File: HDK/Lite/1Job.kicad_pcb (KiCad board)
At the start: 2 copper layers, 48 x 48 mm, 43 parts, among them J101 USB C, J201 TERM, J301 A1-SEL, J302 SSR, J303 CAN, J304 ANA, J305 PWR, J306 DIO, U101 STM32G030F6Px, U102 STM32G030K6Tx, U103 AMS1117-3.3, U104 CH340N, U105 USBLC6-4SC6, U201 SN65HVD230, U202 MCP2518FD, U301 KAQY214, Y201 40MHz

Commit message: updated 1 Job, WIP
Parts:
- removed C106: 100n, Capacitor_SMD:C_0603_1608Metric
- removed D101: 1N4148W, Diode_SMD:D_SOD-123
- removed J101: USB C, Connector_USB:USB_C_Receptacle_HRO_TYPE-C-31-M-12
- removed J302: SSR, Connector_JST:JST_XH_B2B-XH-AM_1x02_P2.50mm_Vertical
- removed J303: CAN, Connector_JST:JST_XH_B2B-XH-AM_1x02_P2.50mm_Vertical
- removed J304: ANA, Connector_JST:JST_PH_S3B-PH-K_1x03_P2.00mm_Horizontal
- removed J305: PWR, Connector_JST:JST_XH_B2B-XH-AM_1x02_P2.50mm_Vertical
- removed J306: DIO, Connector_JST:JST_PH_S3B-PH-K_1x03_P2.00mm_Horizontal
- removed R101, R102, R103, R104, R302, R303, R304, R306: 5.1k, Resistor_SMD:R_0603_1608Metric
- removed R301, R305: 10k, Resistor_SMD:R_0603_1608Metric
- removed R307: 330, Resistor_SMD:R_0603_1608Metric
- removed the REF** at (117.0, 106.8)
- removed U103: AMS1117-3.3, Package_TO_SOT_SMD:SOT-223-3_TabPin2
- removed U104: CH340N, Package_SO:SOIC-8_3.9x4.9mm_P1.27mm
- removed U105: USBLC6-4SC6, Package_TO_SOT_SMD:SOT-23-6
- removed U301: KAQY214, Package_SO:SOP-4_3.8x4.1mm_P2.54mm
- added C401: 100n, Capacitor_SMD:C_0603_1608Metric, F.Cu at (108.1, 103.0)
- added D401: B5819W, Diode_SMD:D_SOD-123, F.Cu at (102.0, 115.8)
- added D402: B5819W, Diode_SMD:D_SOD-123, F.Cu at (110.7, 111.8)
- added J401: SSR, Connector_JST:JST_PH_S2B-PH-K_1x02_P2.00mm_Horizontal, F.Cu at (110.8, 80.5)
- added J402: CAN, Connector_JST:JST_PH_S2B-PH-K_1x02_P2.00mm_Horizontal, F.Cu at (87.2, 119.5)
- added J403: ANA, Connector_JST:JST_PH_S3B-PH-K_1x03_P2.00mm_Horizontal, F.Cu at (102.3, 80.5)
- added J404: PWR, Connector_JST:JST_PH_S2B-PH-K_1x02_P2.00mm_Horizontal, F.Cu at (100.4, 119.5)
- added J405: DIO, Connector_JST:JST_PH_S3B-PH-K_1x03_P2.00mm_Horizontal, F.Cu at (92.0, 80.5)
- added J406: A1-SEL, Connector_PinHeader_2.54mm:PinHeader_1x03_P2.54mm_Vertical, F.Cu at (102.8, 84.9)
- added J407: USB C, Connector_USB:USB_C_Receptacle_HRO_TYPE-C-31-M-12, F.Cu at (121.5, 107.5)
- added R401: 10k, Resistor_SMD:R_0603_1608Metric, F.Cu at (102.4, 88.4)
- added R402: 5.1k, Resistor_SMD:R_0603_1608Metric, F.Cu at (102.4, 90.0)
- added R403: 5.1k, Resistor_SMD:R_0603_1608Metric, F.Cu at (102.4, 91.6)
- added R404: 5.1k, Resistor_SMD:R_0603_1608Metric, F.Cu at (99.0, 88.4)
- added R405: 10k, Resistor_SMD:R_0603_1608Metric, F.Cu at (99.0, 91.6)
- added R406: 5.1k, Resistor_SMD:R_0603_1608Metric, F.Cu at (99.0, 90.0)
- added R407: 330, Resistor_SMD:R_0603_1608Metric, F.Cu at (107.4, 91.3)
- added R408: 5.1k, Resistor_SMD:R_0603_1608Metric, F.Cu at (117.8, 113.8)
- added R409: 5.1k, Resistor_SMD:R_0603_1608Metric, F.Cu at (117.8, 115.4)
- added REF**: SW_SPST_PTS810, Button_Switch_SMD:SW_SPST_PTS810, F.Cu at (103.0, 99.9)
- added U401: KAQY214, Package_SO:SOP-4_3.8x4.1mm_P2.54mm, F.Cu at (107.8, 86.7)
- added U402: CH340N, Package_SO:SOIC-8_3.9x4.9mm_P1.27mm, F.Cu at (110.6, 107.3)
- J301: value A1-SEL -> GT-TF003-H0185-02; footprint Connector_PinHeader_2.54mm:PinHeader_1x03_P2.54mm_Vertical -> Connector_Card:microSD_HC_Molex_104031-0811
- U101: value STM32G030F6Px -> STM32G030K6Tx; footprint Package_SO:TSSOP-20_4.4x6.5mm_P0.65mm -> Package_QFP:LQFP-32_7x7mm_P0.8mm
- U102: value STM32G030K6Tx -> AMS1117-3.3; footprint Package_QFP:LQFP-32_7x7mm_P0.8mm -> Package_TO_SOT_SMD:SOT-223-3_TabPin2
- moved J201 55.2 mm to (95.3, 122.0), turned to 180 degrees
- moved U201 53.7 mm to (88.4, 113.4), turned to -90 degrees
- moved Y201 53.3 mm to (97.0, 104.4)
- moved U202 53.2 mm to (89.0, 104.3), turned to 90 degrees
- moved C201 50.9 mm to (85.2, 99.0), turned to 90 degrees
- moved C202 47.2 mm to (88.5, 108.8)
- moved C104 45.6 mm to (114.7, 122.1), turned to 0 degrees
- moved C105 44.9 mm to (114.5, 120.2), turned to 0 degrees
- moved R201 43.7 mm to (92.0, 115.0), turned to -90 degrees
- moved J301 43.5 mm to (116.9, 90.9), turned to -90 degrees
- moved R202 43.1 mm to (92.6, 120.4), turned to -90 degrees
- moved C204 40.8 mm to (96.7, 101.8)
- moved C203 39.3 mm to (96.7, 107.0)
- moved U102 38.8 mm to (109.3, 118.9), turned to -90 degrees
- moved C102 29.5 mm to (106.2, 113.4), turned to 180 degrees
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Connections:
- net /CanBus/CAN_+ renamed /CAN_+
- net /CanBus/CAN_- renamed /CAN_-
- net /PA0 renamed /ANA_0
- net /PB0 renamed /CAN_CS2
- net /PB3 renamed /PC6
- net /UART2_RX renamed /PA3
- net /UART2_TX renamed /PA2
- C203 pad 1: /CanBus/OSC_OUT -> /CanBus/OSC_IN
- C204 pad 1: /CanBus/OSC_IN -> /CanBus/OSC_OUT
- J301 pad 1: /1JIO/A1_DIV-03V -> unconnected-(J301-DAT2-Pad1)
- J301 pad 2: /1JIO/A1_DIV-12V -> /PA8
- J301 pad 3: /1JIO/A1_DIV-05V -> /PA6
- U101 pad 1: /PB7 -> /I2C1_SDA
- U101 pad 12: /SPI1_SCK -> /PA5
- U101 pad 13: /SPI1_MISO -> /PA6
- U101 pad 14: /SPI1_MOSI -> /PA7
- U101 pad 16: /I2C_SCL -> /DO_SSR
- U101 pad 17: /I2C_SDA -> /PB2
- U101 pad 18: /SWDIO -> /PA8
- U101 pad 19: /SWCLK -> /I2C1_SCL
- U101 pad 8: /PA1 -> /ANA_1
- U102 pad 1: unconnected-(U102-PB9-Pad1) -> GND
- U102 pad 2: unconnected-(U102-PC14-Pad2) -> +3V3
- U102 pad 3: unconnected-(U102-PC15-Pad3) -> VCC
- U202 pad 10: /CanBus/SPI_SCK -> /PB8
- U202 pad 11: /CanBus/SPI_MOSI -> /PB2
- U202 pad 12: /CanBus/SPI_MISO -> /PA10
- U202 pad 13: /CanBus/SPI_CANCS -> /CAN_CS1
- U202 pad 4: unconnected-(U202-~{INT}-Pad4) -> /PB5
- U202 pad 8: unconnected-(U202-~{INT1}/GPIO1-Pad8) -> /CanBus/~{INT1}
- U202 pad 9: unconnected-(U202-~{INT0}/GPIO0/XSTBY-Pad9) -> /CanBus/~{INT0}
- Y201 pad 1: /CanBus/OSC_OUT -> /CanBus/OSC_IN
- Y201 pad 4: /CanBus/OSC_IN -> /CanBus/OSC_OUT
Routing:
- net +3V3: track 0.00 -> 138.1 mm, vias 0 -> 6
- net /PA5: track 0.00 -> 42.6 mm, vias 0 -> 2
- net /PA7: track 0.00 -> 39.9 mm, vias 0 -> 2
- net /PA14: track 0.00 -> 37.0 mm, vias 0 -> 2
- net /PA8: track 0.00 -> 36.9 mm, vias 0 -> 2
- net /PA13: track 0.00 -> 36.5 mm, vias 0 -> 2
- net /PA6: track 0.00 -> 35.8 mm, vias 0 -> 2
- net /SWDIO: track 31.8 -> 0.00 mm, vias 2 -> 0
- net /SWCLK: track 30.6 -> 0.00 mm, vias 2 -> 0
- net /DO_SSR: track 0.00 -> 30.3 mm, vias 0 -> 2
- net GND: track 5.84 -> 33.1 mm, vias 5 -> 19
- net /PB6: track 0.00 -> 22.3 mm, vias 0 -> 2
- net /PB7: track 0.00 -> 22.2 mm, vias 0 -> 2
- net /ANA_1: track 0.00 -> 17.9 mm, vias 0 -> 2
- net /~{NRST}: track 0.00 -> 17.1 mm, vias 0 -> 2
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- added copper zone on F.Cu, net +3V3
- added copper zone on F.Cu, net VCC

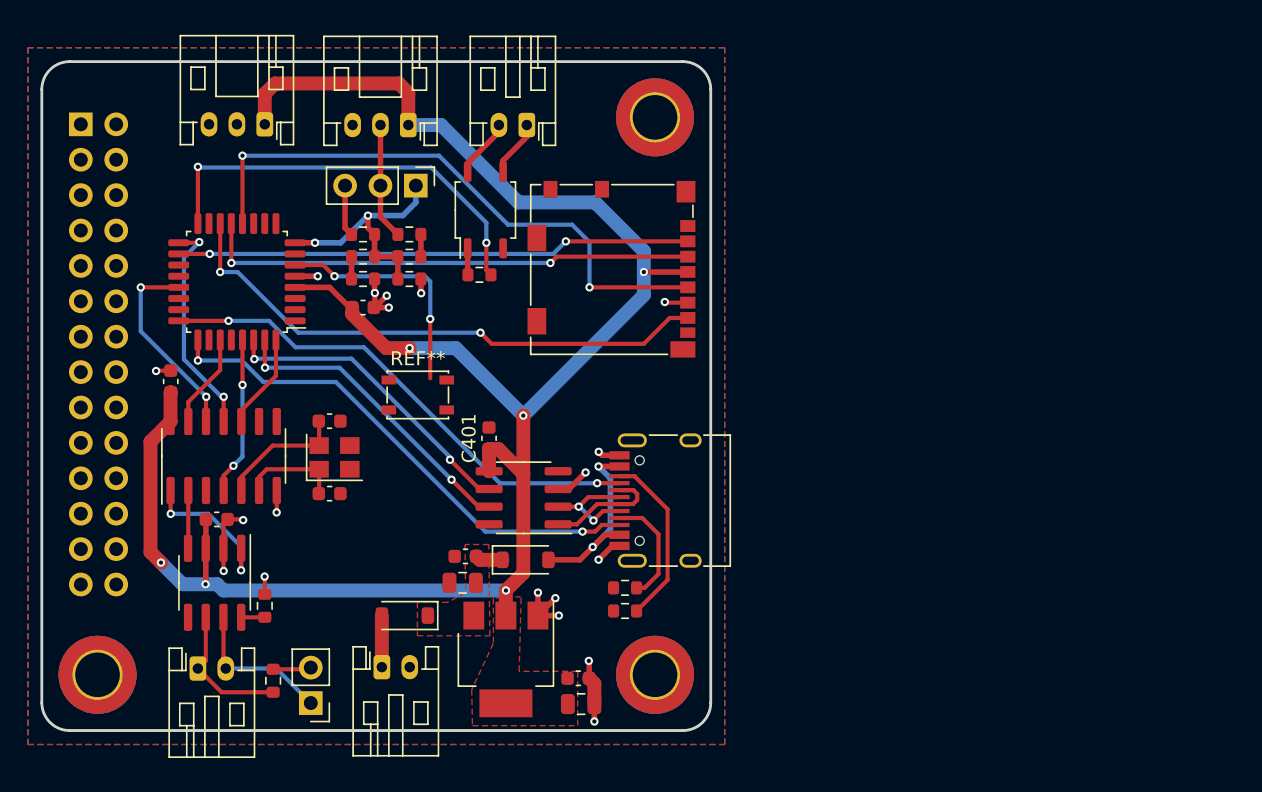
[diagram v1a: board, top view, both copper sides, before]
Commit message: updated 1Job, 75%
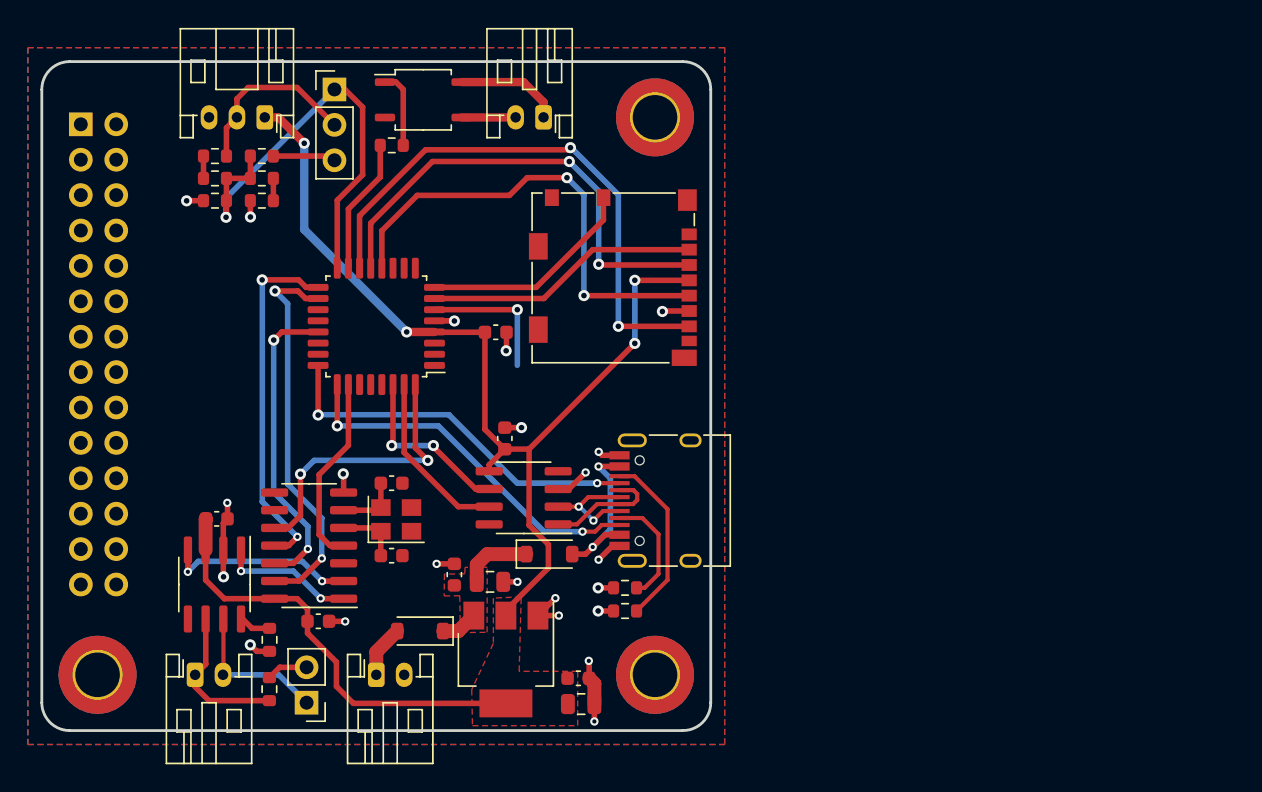
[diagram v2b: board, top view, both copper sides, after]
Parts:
- removed J405: DIO, Connector_JST:JST_PH_S3B-PH-K_1x03_P2.00mm_Horizontal
- removed the REF** at (103.0, 99.9)
- moved C201 20.2 mm to (95.8, 116.2), turned to 0 degrees
- moved R401 15.0 mm to (88.4, 82.8), turned to 180 degrees
- moved R402 15.0 mm to (88.4, 84.4), turned to 0 degrees
- moved R403 15.0 mm to (88.4, 86.0), turned to 0 degrees
- moved R407 11.2 mm to (101.1, 82.0), turned to 0 degrees
- moved U101 10.5 mm to (100.0, 95.0)
- moved J403 10.3 mm to (92.0, 80.0)
- moved C101 9.68 mm to (108.6, 95.4)
- moved R404 9.18 mm to (91.8, 82.8), turned to 180 degrees
- moved R406 9.18 mm to (91.8, 84.4), turned to 180 degrees
- moved R405 9.18 mm to (91.8, 86.0), turned to 0 degrees
- moved U401 9.08 mm to (103.4, 78.7), turned to 0 degrees
- moved J406 9.04 mm to (97.0, 78.0), turned to 0 degrees
- moved U202 8.88 mm to (95.2, 110.7), turned to 180 degrees
- moved C203 6.29 mm to (101.1, 111.5)
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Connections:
- C203 pad 1: /CanBus/OSC_IN -> /CanBus/OSC_OUT
- C204 pad 1: /CanBus/OSC_OUT -> /CanBus/OSC_IN
- J301 pad 2: /PA8 -> /PA0
- J301 pad 9: /SDCARD_DET -> /PA1
- U101 pad 15: /CAN_CS2 -> /DO_SSR
- U101 pad 16: /DO_SSR -> /ANA_1
- U101 pad 18: /PA8 -> /CAN_CS1
- U101 pad 27: /CAN_CS1 -> /PB3
- U101 pad 7: /ANA_0 -> /PA0
- U101 pad 8: /ANA_1 -> /PA1
- U202 pad 4: /PB5 -> /PA15
- U401 pad 3: /1JIO/SSR-IN -> /1JIO/SSR-OUT
- U401 pad 4: /1JIO/SSR-OUT -> /1JIO/SSR-IN
- Y201 pad 1: /CanBus/OSC_IN -> /CanBus/OSC_OUT
- Y201 pad 4: /CanBus/OSC_OUT -> /CanBus/OSC_IN
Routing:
- net /PA8: track 36.9 -> 0.00 mm, vias 2 -> 0
- net +3V3: track 138.1 -> 103.2 mm, vias 6 -> 4
- net /CAN_CS1: track 6.80 -> 28.0 mm, vias 0 -> 2
- net /DO_SSR: track 30.3 -> 9.76 mm, vias 2 -> 0
- net /PA0: track 0.00 -> 19.7 mm
- net /PA1: track 0.00 -> 15.7 mm
- net /ANA_1: track 17.9 -> 33.4 mm, vias 2 -> 1
- net /PA15: track 0.00 -> 13.7 mm
- net /PB8: track 6.88 -> 20.6 mm, vias 0 -> 2
- net /PB5: track 11.4 -> 0.00 mm, vias 2 -> 0
- net /PA14: track 37.0 -> 26.6 mm
- net /PB7: track 22.2 -> 12.6 mm, vias 2 -> 0
- net /PB2: track 16.1 -> 25.6 mm
- net /PB6: track 22.3 -> 12.7 mm
- net /CanBus/CAN_RX: track 4.16 -> 13.6 mm, vias 0 -> 2
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
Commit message: updated 1 Job, 85%
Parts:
- added kibuzzard-654FB514: G***, kibuzzard-654FB514, F.Cu at (117.0, 100.2)
- added kibuzzard-654FB554: G***, kibuzzard-654FB554, F.Cu at (92.1, 90.7)
- added kibuzzard-654FB568: G***, kibuzzard-654FB568, F.Cu at (89.7, 89.0)
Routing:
- net /PA2: track 0.00 -> 23.4 mm, vias 0 -> 1
- net /PA3: track 0.00 -> 23.3 mm, vias 0 -> 1
- net /PA4: track 0.00 -> 19.2 mm, vias 0 -> 1
- net /I2C1_SDA: track 0.00 -> 19.0 mm, vias 0 -> 2
- net /PB5: track 0.00 -> 18.2 mm, vias 0 -> 2
- net /PB4: track 0.00 -> 16.0 mm, vias 0 -> 2
- net /PB3: track 0.00 -> 14.1 mm, vias 0 -> 2
- net /PC6: track 0.00 -> 10.1 mm
- net /I2C1_SCL: track 0.00 -> 9.87 mm
- net /PA14: track 26.6 -> 35.8 mm
- net +3V3: track 103.2 -> 110.1 mm
- net /PA13: track 27.2 -> 33.7 mm
- net /I2C2_SCL: track 0.00 -> 6.12 mm
- net /I2C2_SDA: track 0.00 -> 5.59 mm
- net /PB6: track 12.7 -> 11.9 mm
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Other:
- board text added: "1"
- board text added: "JLCJLCJLCJLC"
- board text added: "blame: scottcjx.w@gmail.com"

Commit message: updated 1-Job, v1rA
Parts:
- removed J301: GT-TF003-H0185-02, Connector_Card:microSD_HC_Molex_104031-0811
- added D101: LED, LED_SMD:LED_0603_1608Metric, F.Cu at (105.8, 87.9)
- added D102: LED, LED_SMD:LED_0603_1608Metric, F.Cu at (116.8, 115.3)
- added G***: LOGO, scottcjx-graphics:nvf_30mm, B.Cu at (102.1, 99.5)
- added J302: DM3CS-SF, footprints:HRS_DM3CS-SF, F.Cu at (115.8, 91.4)
- added R101: 10k, Resistor_SMD:R_0603_1608Metric, F.Cu at (105.8, 89.6)
- added R102: 10k, Resistor_SMD:R_0603_1608Metric, F.Cu at (115.0, 115.4)
- added kibuzzard-654FB554: G***, kibuzzard-654FB554, B.Cu at (108.3, 85.1)
- added kibuzzard-654FB568: G***, kibuzzard-654FB568, B.Cu at (110.7, 83.4)
- added kibuzzard-6550DE2D: G***, kibuzzard-6550DE2D, B.Cu at (97.4, 108.2)
- C203, C204: value 10p -> 20p
- J201: footprint Connector_PinHeader_2.54mm:PinHeader_1x02_P2.54mm_Vertical -> Connector_PinHeader_2.54mm:PinHeader_1x02_P2.54mm_Horizontal
- J401, J402, J404: footprint Connector_JST:JST_PH_S2B-PH-K_1x02_P2.00mm_Horizontal -> NVF-Kicad:JST-PH-1x02-Horizontal
- J403: footprint Connector_JST:JST_PH_S3B-PH-K_1x03_P2.00mm_Horizontal -> NVF-Kicad:JST-PH-1x03-Horizontal
- J405: renamed from REF**; value 48x48 Module -> Conn_02x14_Odd_Even
- J406: footprint Connector_PinHeader_2.54mm:PinHeader_1x03_P2.54mm_Vertical -> Connector_PinHeader_2.54mm:PinHeader_1x03_P2.54mm_Horizontal
- J407: footprint Connector_USB:USB_C_Receptacle_HRO_TYPE-C-31-M-12 -> NVF-Kicad:USB_C_Receptacle_HRO_TYPE-C-31-M-12
- moved R202 9.83 mm to (83.9, 116.0), turned to 0 degrees
- moved U401 6.65 mm to (99.8, 84.3)
- moved R407 6.60 mm to (97.5, 87.5)
- moved R409 3.61 mm to (121.3, 114.5), turned to -90 degrees
- moved J201 2.80 mm to (96.3, 119.5), turned to -90 degrees
- moved J406 2.46 mm to (98.5, 80.0), turned to 90 degrees
- moved C101 2.04 mm to (106.7, 96.2), turned to -90 degrees
- moved R408 1.98 mm to (119.7, 114.5), turned to -90 degrees
- moved R201 1.38 mm to (92.7, 116.2), turned to 180 degrees
- moved C203 1.19 mm to (101.8, 112.5), turned to 180 degrees
- moved J404 1.00 mm to (101.0, 120.0)
- moved Y201 0.67 mm to (101.7, 109.5), turned to 90 degrees
- moved C204 0.51 mm to (101.6, 106.4)
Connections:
- J201 pad 1: /CAN_+ -> Net-(J201-Pin_1)
- J201 pad 2: Net-(J201-Pin_2) -> /CAN_+
- J401 pad 1: /1JIO/SSR-IN -> /1JIO/SSR-OUT
- J401 pad 2: /1JIO/SSR-OUT -> /1JIO/SSR-IN
- J405 pad 1: (no net) -> +3V3
- J405 pad 10: (no net) -> /PA6
- J405 pad 11: (no net) -> /I2C2_SDA
- J405 pad 12: (no net) -> /PA7
- J405 pad 13: (no net) -> /I2C2_SCL
- J405 pad 14: (no net) -> /PB8
- J405 pad 15: (no net) -> /PB3
- J405 pad 16: (no net) -> /PB2
- J405 pad 17: (no net) -> /PB4
- J405 pad 18: (no net) -> /PA10
- J405 pad 19: (no net) -> /PB5
- J405 pad 2: (no net) -> GND
- J405 pad 20: (no net) -> /PA13
- J405 pad 21: (no net) -> /PB6
- J405 pad 22: (no net) -> /PA14
- J405 pad 23: (no net) -> /PB7
- J405 pad 24: (no net) -> +3V3
- J405 pad 25: (no net) -> GND
- J405 pad 26: (no net) -> GND
- J405 pad 27: (no net) -> /~{NRST}
- J405 pad 28: (no net) -> VCC
- J405 pad 3: (no net) -> unconnected-(J405-Pin_3-Pad3)
- J405 pad 4: (no net) -> /PA3
- J405 pad 5: (no net) -> unconnected-(J405-Pin_5-Pad5)
- J405 pad 6: (no net) -> /PA2
- J405 pad 7: (no net) -> /I2C1_SDA
- J405 pad 8: (no net) -> /PA5
- J405 pad 9: (no net) -> /I2C1_SCL
- J407 pad A8: /PA13 -> /PA14
- J407 pad B8: /PA14 -> /PA13
- R202 pad 1: Net-(J201-Pin_2) -> Net-(J201-Pin_1)
- Y201 pad 3: GND -> /CanBus/OSC_IN
- Y201 pad 4: /CanBus/OSC_IN -> GND
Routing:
- net /~{NRST}: track 9.94 -> 69.2 mm, vias 1 -> 2
- net /PB7: track 12.6 -> 53.1 mm, vias 0 -> 1
- net +3V3: track 110.1 -> 141.2 mm, vias 4 -> 3
- net VCC: track 7.76 -> 35.0 mm, vias 0 -> 1
- net /PB6: track 11.9 -> 37.6 mm, vias 2 -> 3
- net /PB8: track 20.2 -> 39.4 mm, vias 2 -> 3
- net /I2C1_SDA: track 19.0 -> 37.2 mm, vias 2 -> 4
- net Net-(J201-Pin_1): track 0.00 -> 18.0 mm
- net /PA13: track 33.7 -> 51.3 mm
- net /PA5: track 34.1 -> 50.2 mm, vias 2 -> 4
- net /PA6: track 34.1 -> 49.1 mm, vias 2 -> 5
- net /PA10: track 22.5 -> 36.2 mm
- net /I2C2_SCL: track 6.12 -> 19.8 mm, vias 0 -> 2
- net /I2C2_SDA: track 5.59 -> 18.9 mm, vias 0 -> 1
- net /PB2: track 25.6 -> 38.8 mm
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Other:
- board text added: "+"
- board text added: "10k"
- board text added: "3v3"
- board text added: "5-12V"
- board text added: "5v"
- board text added: "CAN"
- board text added: "IO"
- board text added: "QC"
- board text added: "SN"
- board text added: "SSR"
- board text added: "Scott CJX, 2023 scottcjx.github.io/1-Job blame: scottcjx.w@gmail.com"
- board text added: "V_{max}"
- board text added: "pwr"
- board text added: "term"
- board text added: "usr"
- board text removed: "blame: scottcjx.w@gmail.com"
